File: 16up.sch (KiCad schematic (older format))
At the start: 38 parts, among them CN1 EXPANSION_PORT, CN2 ALMOST_USERPORT, CN3 DB9_MALE, J1 ATTENTION_IN, J2 TAPE_IN, U1 GAL20V8, U102 74LS652, U2 MOS_6529, U3 MOS_6551_ACIA, U4 MAX238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

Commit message: ExtraUserPort -> 16up
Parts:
- CN1: footprint ExtraUserPort:C16_Cart_Conn -> 16up:C16_Cart_Conn
- CN2: footprint ExtraUserPort:24Pin_Edge -> 16up:24Pin_Edge
- CN3: footprint ExtraUserPort:DB_9M -> 16up:DB_9M
- J2: footprint ExtraUserPort:Connector_Mini-DIN_Female_8Pin_2rows -> 16up:Connector_Mini-DIN_Female_8Pin_2rows
- V0: footprint ExtraUserPort:logo -> 16up:logo
- V1: footprint ExtraUserPort:cc_by_nc_sa -> 16up:cc_by_nc_sa
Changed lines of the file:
@@
 encoding utf-8
 Sheet 1 1
-Title "ExtraUserPort"
+Title "16up"
 Date "2022-09-17"
 Rev "1git"
@@
 F 0 "CN2" H 14315 2680 50  0000 C CNN
 F 1 "ALMOST_USERPORT" H 14315 2589 50  0000 C CNN
-F 2 "ExtraUserPort:24Pin_Edge" H 14315 1765 50  0001 C CNN
+F 2 "16up:24Pin_Edge" H 14315 1765 50  0001 C CNN
 F 3 "DOCUMENTATION" H 14315 1765 50  0001 C CNN
 	1    14315 1765
@@
 F 0 "CN3" H 14538 8742 50  0000 C CNN
 F 1 "DB9_MALE" H 14538 8651 50  0000 C CNN
-F 2 "ExtraUserPort:DB_9M" H 14620 8050 50  0001 C CNN
+F 2 "16up:DB_9M" H 14620 8050 50  0001 C CNN
 F 3 " ~" H 14620 8050 50  0001 C CNN
 	1    14620 8050
@@
 F 0 "CN1" H 2435 4370 50  0000 C CNN
 F 1 "EXPANSION_PORT" H 2435 4279 50  0000 C CNN
-F 2 "ExtraUserPort:C16_Cart_Conn" H 2435 1155 50  0001 C CNN
+F 2 "16up:C16_Cart_Conn" H 2435 1155 50  0001 C CNN
 F 3 "DOCUMENTATION" H 2435 1055 50  0001 C CNN
 	1    2435 2805
@@
 F 0 "J2" H 6040 9780 50  0000 C CNN
 F 1 "TAPE_IN" H 6040 9685 50  0000 C CNN
-F 2 "ExtraUserPort:Connector_Mini-DIN_Female_8Pin_2rows" V 5780 10050 50  0001 C CNN
+F 2 "16up:Connector_Mini-DIN_Female_8Pin_2rows" V 5780 10050 50  0001 C CNN
 F 3 "http://service.powerdynamics.com/ec/Catalog17/Section%2011.pdf" V 5780 10050 50  0001 C CNN
 	1    5790 10060
@@
 F 0 "V0" H 11078 11071 50  0000 L CNN
 F 1 "LOGO" H 11078 10980 50  0000 L CNN
-F 2 "ExtraUserPort:logo" H 11000 11025 50  0001 C CNN
+F 2 "16up:logo" H 11000 11025 50  0001 C CNN
 F 3 "" H 11000 11025 50  0001 C CNN
 	1    11000 11025
@@
 F 0 "V1" H 11078 10846 50  0000 L CNN
 F 1 "CC-BY-NC-SA" H 11078 10755 50  0000 L CNN
-F 2 "ExtraUserPort:cc_by_nc_sa" H 11000 10800 50  0001 C CNN
+F 2 "16up:cc_by_nc_sa" H 11000 10800 50  0001 C CNN
 F 3 "" H 11000 10800 50  0001 C CNN
 	1    11000 10800

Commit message: Fix userport connector !!!
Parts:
- CN2: footprint 16up:24Pin_Edge -> 16up:Plus4_UserPort
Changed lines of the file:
@@
 F 0 "CN2" H 14315 2680 50  0000 C CNN
 F 1 "ALMOST_USERPORT" H 14315 2589 50  0000 C CNN
-F 2 "16up:24Pin_Edge" H 14315 1765 50  0001 C CNN
+F 2 "16up:Plus4_UserPort" H 14315 1765 50  0001 C CNN
 F 3 "DOCUMENTATION" H 14315 1765 50  0001 C CNN
 	1    14315 1765

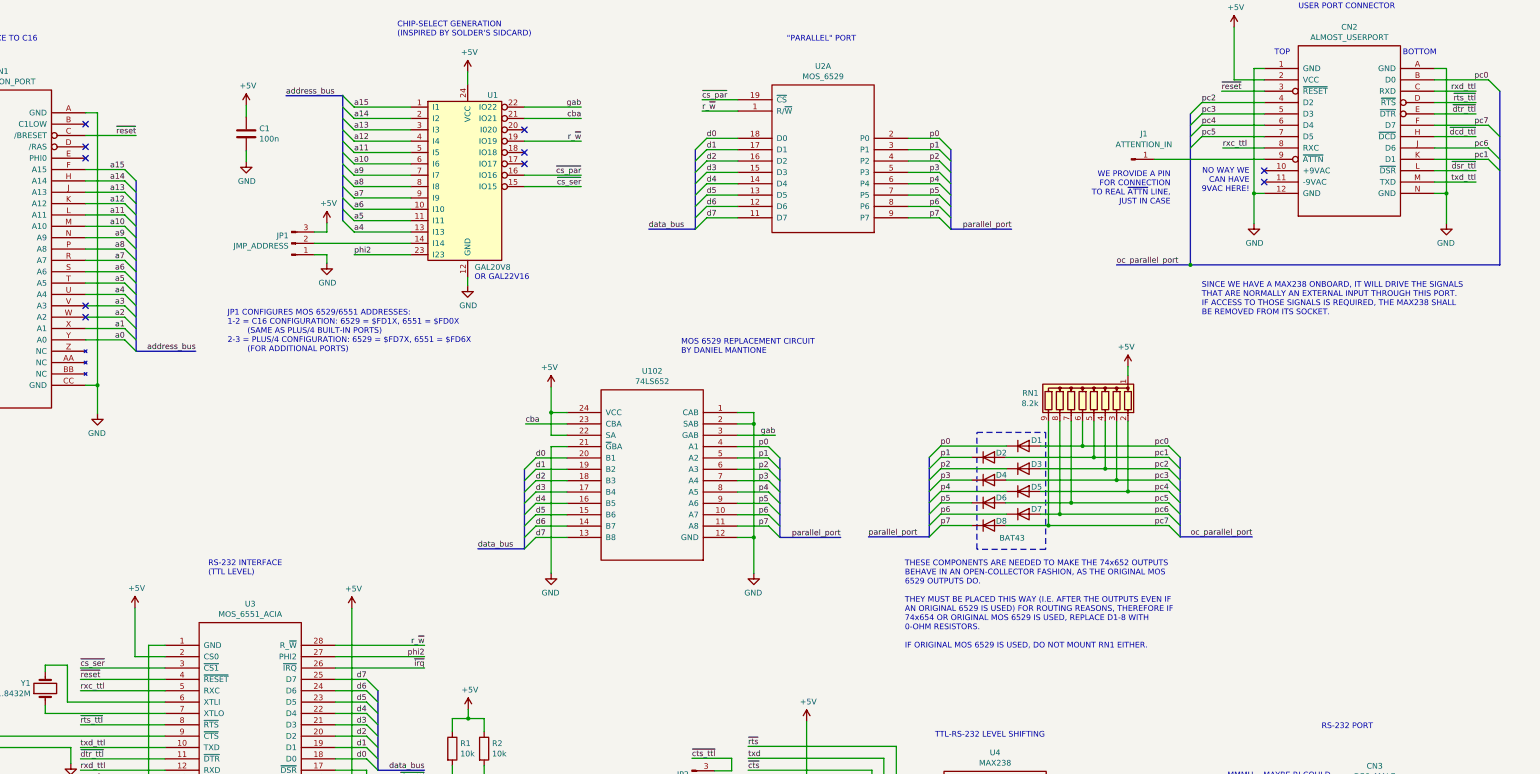
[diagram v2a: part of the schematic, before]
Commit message: Remove serial signals from Userport connector They wouldn't work anyway, as whatever gets connected there expects all control signals to be inverted as per Commodore serial port standards.
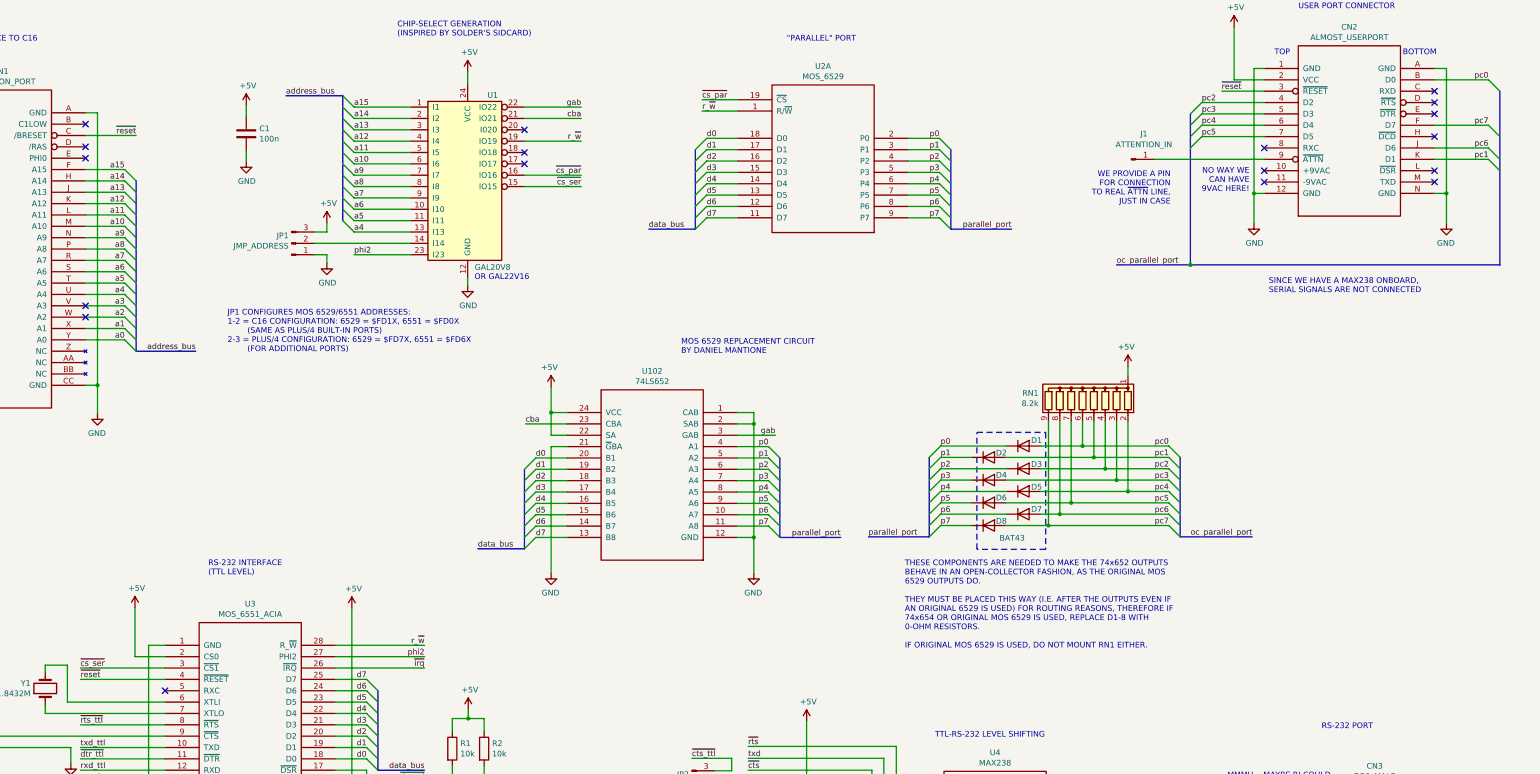
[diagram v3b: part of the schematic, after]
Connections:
- net rxd_ttl: no longer CN2.C (RXD)
- net txd_ttl: no longer CN2.M (TXD)
- net ~dcd_ttl: no longer CN2.H (~DCD)
- net ~dsr_ttl: no longer CN2.L (~DSR)
- net ~dtr_ttl: no longer CN2.E (~DTR)
- net ~rts_ttl: no longer CN2.D (~RTS)
- net rxc_ttl: no longer names the net of CN2.8 (RXC)
- net rxc_ttl: no longer U3.5 (RXC)
- no-connect marks 29 -> 37
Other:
- note added: "SINCE WE HAVE A MAX238 ONBOARD,\nSERIAL SIGNALS ARE NOT CONNECTED"
- note removed: "SINCE WE HAVE A MAX238 ONBOARD, IT WILL DRIVE THE SIGNALS\nTHAT ARE NORMALLY AN EXTERNAL INPUT THROUGH THIS PORT.\nIF ACCESS TO THOSE SIGNALS IS REQUIRED, THE MAX238 SHALL\nBE REMOVED FROM ITS SOCKET."
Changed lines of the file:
@@
 Sheet 1 1
 Title "16up"
-Date "2022-09-17"
+Date "2022-09-21"
 Rev "1git"
 Comp "SukkoPera & The Folks From The Plus/4 World Forum"
@@
 Wire Wire Line
 	14320 8250 13840 8250
-Wire Wire Line
-	15065 1815 15430 1815
-Wire Wire Line
-	15065 2115 15430 2115
-Text Label 15430 1815 2    50   ~ 0
-~dcd_ttl
-Text Label 15430 2115 2    50   ~ 0
-~dsr_ttl
-Wire Wire Line
-	15065 2215 15430 2215
-Text Label 15430 2215 2    50   ~ 0
-txd_ttl
 Wire Wire Line
 	14320 8350 13840 8350
@@
 Text Notes 13865 700  0    50   ~ 0
 USER PORT CONNECTOR
-Wire Wire Line
-	13565 1915 13200 1915
-Text Label 13200 1915 0    50   ~ 0
-rxc_ttl
 Text Notes 10665 7115 0    50   ~ 0
 TTL-RS-232 LEVEL SHIFTING
@@
 Wire Wire Line
 	1240 4005 1580 4005
-Text Label 15430 1615 2    50   ~ 0
-~dtr_ttl
-Text Label 15430 1515 2    50   ~ 0
-~rts_ttl
-Text Label 15430 1415 2    50   ~ 0
-rxd_ttl
-Wire Wire Line
-	15065 1615 15430 1615
-Wire Wire Line
-	15065 1515 15430 1515
-Wire Wire Line
-	15065 1415 15430 1415
-Text Notes 13015 3395 0    50   ~ 0
-SINCE WE HAVE A MAX238 ONBOARD, IT WILL DRIVE THE SIGNALS\nTHAT ARE NORMALLY AN EXTERNAL INPUT THROUGH THIS PORT.\nIF ACCESS TO THOSE SIGNALS IS REQUIRED, THE MAX238 SHALL\nBE REMOVED FROM ITS SOCKET.
+Text Notes 13605 3200 0    50   ~ 0
+SINCE WE HAVE A MAX238 ONBOARD,\nSERIAL SIGNALS ARE NOT CONNECTED
 $Comp
 L Connector:Conn_01x03_Male JP2
@@
 Entry Wire Line
 	3140 7595 3240 7495
-Wire Wire Line
-	3140 6695 3885 6695
-Text Label 3140 6695 0    50   ~ 0
-rxc_ttl
 Wire Wire Line
 	3140 6595 3885 6595
@@
 Text Notes 6350 10750 0    50   ~ 0
 THE IDEA HERE IS TO USE A Y-CABLE AND CONNECT\nTHE DATASSETTE BOTH TO THE ORIGINAL PORT AND TO\nTHIS ONE, SO THAT WE CAN PUT THE SENSE SIGNAL ON\nD2 WHEN REQUIRED.\n\nIDEALLY THE SENSE LINE SHOULD BE BROUGHT HERE\nONLY, BUT PROBABLY IT WON'T HARM ANYWAY.\n\n
+NoConn ~ 13565 1915
+NoConn ~ 15065 1415
+NoConn ~ 15065 1515
+NoConn ~ 15065 1615
+NoConn ~ 15065 1815
+NoConn ~ 15065 2115
+NoConn ~ 15065 2215
+NoConn ~ 3885 6695
 Wire Bus Line
 	15640 1415 15640 2945

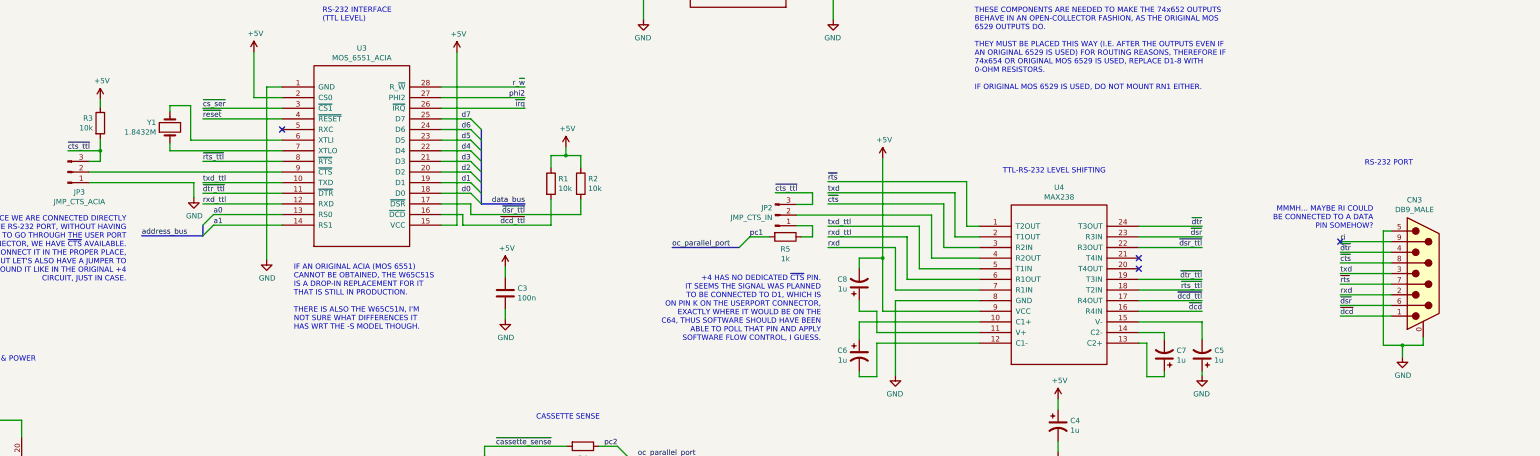
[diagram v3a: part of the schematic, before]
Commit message: Pull-up signals at the RS-232 port
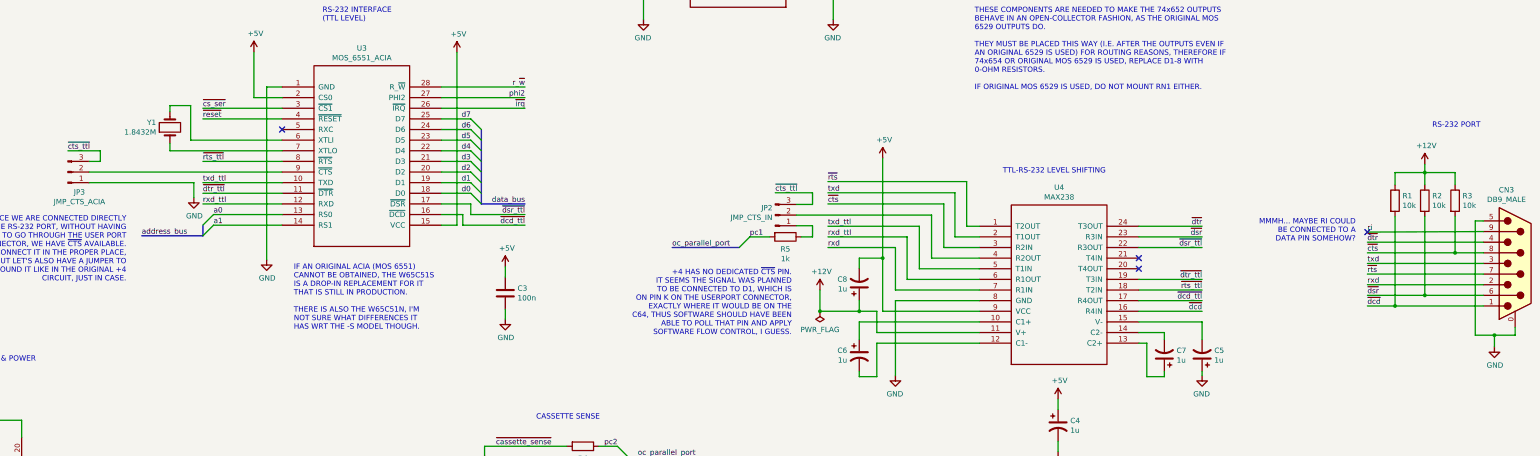
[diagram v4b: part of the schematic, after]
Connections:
- net +5V: no longer R1.1, R2.1, R3.1
- net ~cts: now also R3.2
- net ~cts_ttl: no longer R3.2
- net ~dcd: now also R1.2
- net ~dcd_ttl: no longer R1.2
- net ~dsr: now also R2.2
- net ~dsr_ttl: no longer R2.2
- net +12V: now reaches C8.1, U4.11 (V+)
- net +12V: now also R1.1, R2.1, R3.1
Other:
- note added: "MMMH... MAYBE RI COULD\nBE CONNECTED TO A\nDATA PIN SOMEHOW?"
- note removed: "MMMH... MAYBE RI COULD\nBE CONNECTED TO A DATA\nPIN SOMEHOW?"
- moved on the sheet: CN3, R1, R2, R3
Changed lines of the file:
@@
 Sheet 1 1
 Title "16up"
-Date "2022-09-21"
+Date "2022-09-29"
 Rev "1git"
 Comp "SukkoPera & The Folks From The Plus/4 World Forum"
@@
 L Connector:DB9_Male_MountingHoles CN?
 U 1 1 647E28B3
-P 14620 8050
+P 15485 7955
 AR Path="/647386BE/647E28B3" Ref="CN?"  Part="1"
 AR Path="/647E28B3" Ref="CN3"  Part="1"
-F 0 "CN3" H 14538 8742 50  0000 C CNN
-F 1 "DB9_MALE" H 14538 8651 50  0000 C CNN
-F 2 "16up:DB_9M" H 14620 8050 50  0001 C CNN
-F 3 " ~" H 14620 8050 50  0001 C CNN
-	1    14620 8050
-	1    0    0    -1
-$EndComp
-Wire Wire Line
-	14320 7650 14245 7650
-Wire Wire Line
-	14245 7650 14245 8725
-Wire Wire Line
-	14245 8725 14425 8725
-Wire Wire Line
-	14620 8725 14620 8650
-Wire Wire Line
-	14425 8725 14425 8835
-Connection ~ 14425 8725
-Wire Wire Line
-	14425 8725 14620 8725
+F 0 "CN3" H 15403 8647 50  0000 C CNN
+F 1 "DB9_MALE" H 15403 8556 50  0000 C CNN
+F 2 "16up:DB_9M" H 15485 7955 50  0001 C CNN
+F 3 " ~" H 15485 7955 50  0001 C CNN
+	1    15485 7955
+	1    0    0    -1
+$EndComp
+Wire Wire Line
+	15185 7555 15110 7555
+Wire Wire Line
+	15110 7555 15110 8630
+Wire Wire Line
+	15110 8630 15290 8630
+Wire Wire Line
+	15485 8630 15485 8555
+Wire Wire Line
+	15290 8630 15290 8740
+Connection ~ 15290 8630
+Wire Wire Line
+	15290 8630 15485 8630
 $Comp
 L power:GND #PWR?
 U 1 1 647E28C7
-P 14425 8835
+P 15290 8740
 AR Path="/647386BE/647E28C7" Ref="#PWR?"  Part="1"
 AR Path="/647E28C7" Ref="#PWR0118"  Part="1"
-F 0 "#PWR0118" H 14425 8585 50  0001 C CNN
-F 1 "GND" H 14430 8662 50  0000 C CNN
-F 2 "" H 14425 8835 50  0001 C CNN
-F 3 "" H 14425 8835 50  0001 C CNN
-	1    14425 8835
-	1    0    0    -1
-$EndComp
-Wire Wire Line
-	14320 8050 13840 8050
-Wire Wire Line
-	14320 7950 13840 7950
-Wire Wire Line
-	14320 7750 13840 7750
-Text Label 13840 8450 0    50   ~ 0
+F 0 "#PWR0118" H 15290 8490 50  0001 C CNN
+F 1 "GND" H 15295 8567 50  0000 C CNN
+F 2 "" H 15290 8740 50  0001 C CNN
+F 3 "" H 15290 8740 50  0001 C CNN
+	1    15290 8740
+	1    0    0    -1
+$EndComp
+Wire Wire Line
+	15185 7655 14095 7660
+Text Label 14095 8355 0    50   ~ 0
 ~dcd
-Text Label 13840 8250 0    50   ~ 0
+Text Label 14095 8155 0    50   ~ 0
 rxd
-Text Label 13840 8050 0    50   ~ 0
+Text Label 14095 7955 0    50   ~ 0
 txd
-Text Label 13840 7850 0    50   ~ 0
+Text Label 14095 7755 0    50   ~ 0
 ~dtr
-Text Label 13840 8350 0    50   ~ 0
+Text Label 14095 8255 0    50   ~ 0
 ~dsr
-Text Label 13840 8150 0    50   ~ 0
+Text Label 14095 8055 0    50   ~ 0
 ~rts
-Text Label 13840 7950 0    50   ~ 0
+Text Label 14095 7855 0    50   ~ 0
 ~cts
-Text Label 13840 7750 0    50   ~ 0
+Text Label 14095 7660 0    50   ~ 0
 ri
-NoConn ~ 13840 7750
-Wire Wire Line
-	14320 7850 13840 7850
-Wire Wire Line
-	14320 8150 13840 8150
-Wire Wire Line
-	14320 8250 13840 8250
-Wire Wire Line
-	14320 8350 13840 8350
-Wire Wire Line
-	14320 8450 13840 8450
+NoConn ~ 14095 7660
 Connection ~ 12915 2945
 Wire Wire Line
@@
 Text Notes 10665 7115 0    50   ~ 0
 TTL-RS-232 LEVEL SHIFTING
-Text Notes 14070 7040 0    50   ~ 0
+Text Notes 14705 6685 0    50   ~ 0
 RS-232 PORT
 Text Notes 13435 2310 2    50   ~ 0
@@
 	1    0    0    1
 $EndComp
-Text Notes 14150 7635 2    50   ~ 0
-MMMH... MAYBE RI COULD\nBE CONNECTED TO A DATA\nPIN SOMEHOW?
+Text Notes 13985 7755 2    50   ~ 0
+MMMH... MAYBE RI COULD\nBE CONNECTED TO A\nDATA PIN SOMEHOW?
 Wire Wire Line
 	8725 7400 8875 7400
@@
 Text Label 7555 7805 0    50   ~ 0
 oc_parallel_port
-Text Notes 8955 8690 2    50   ~ 0
+Text Notes 8680 8635 2    50   ~ 0
 +4 HAS NO DEDICATED ~CTS~ PIN.\nIT SEEMS THE SIGNAL WAS PLANNED\nTO BE CONNECTED TO D1, WHICH IS\nON PIN K ON THE USERPORT CONNECTOR,\nEXACTLY WHERE IT WOULD BE ON THE\nC64, THUS SOFTWARE SHOULD HAVE BEEN\nABLE TO POLL THAT PIN AND APPLY\nSOFTWARE FLOW CONTROL, I GUESS.
 Wire Wire Line
@@
 Wire Wire Line
 	5660 7395 5660 7495
-$Comp
-L power:+5V #PWR0126
-U 1 1 6524739E
-P 6555 6860
-F 0 "#PWR0126" H 6555 6710 50  0001 C CNN
-F 1 "+5V" H 6570 7033 50  0000 C CNN
-F 2 "" H 6555 6860 50  0001 C CNN
-F 3 "" H 6555 6860 50  0001 C CNN
-	1    6555 6860
-	1    0    0    -1
-$EndComp
-Wire Wire Line
-	6555 6940 6695 6940
-Connection ~ 6555 6940
-Wire Wire Line
-	6555 6940 6555 6860
-Wire Wire Line
-	6695 6940 6695 7055
-Wire Wire Line
-	6415 6940 6555 6940
-Wire Wire Line
-	6415 7055 6415 6940
-Wire Wire Line
-	6415 7355 6415 7595
+Wire Wire Line
+	14355 7215 14355 7100
 Wire Wire Line
 	5530 5970 5530 7595
-Wire Wire Line
-	6695 7355 6695 7495
 $Comp
 L Device:R R2
 U 1 1 64D53226
-P 6695 7205
-F 0 "R2" H 6765 7251 50  0000 L CNN
-F 1 "10k" H 6765 7160 50  0000 L CNN
-F 2 "Resistor_THT:R_Axial_DIN0207_L6.3mm_D2.5mm_P2.54mm_Vertical" V 6625 7205 50  0001 C CNN
-F 3 "~" H 6695 7205 50  0001 C CNN
-	1    6695 7205
+P 14635 7365
+F 0 "R2" H 14705 7411 50  0000 L CNN
+F 1 "10k" H 14705 7320 50  0000 L CNN
+F 2 "Resistor_THT:R_Axial_DIN0207_L6.3mm_D2.5mm_P2.54mm_Vertical" V 14565 7365 50  0001 C CNN
+F 3 "~" H 14635 7365 50  0001 C CNN
+	1    14635 7365
 	1    0    0    -1
 $EndComp
@@
 L Device:R R1
 U 1 1 64D5229C
-P 6415 7205
-F 0 "R1" H 6485 7251 50  0000 L CNN
-F 1 "10k" H 6485 7160 50  0000 L CNN
-F 2 "Resistor_THT:R_Axial_DIN0207_L6.3mm_D2.5mm_P2.54mm_Vertical" V 6345 7205 50  0001 C CNN
-F 3 "~" H 6415 7205 50  0001 C CNN
-	1    6415 7205
+P 14355 7365
+F 0 "R1" H 14425 7411 50  0000 L CNN
+F 1 "10k" H 14425 7320 50  0000 L CNN
+F 2 "Resistor_THT:R_Axial_DIN0207_L6.3mm_D2.5mm_P2.54mm_Vertical" V 14285 7365 50  0001 C CNN
+F 3 "~" H 14355 7365 50  0001 C CNN
+	1    14355 7365
 	1    0    0    -1
 $EndComp
@@
 	3140 7295 3885 7295
 Wire Wire Line
-	5660 7495 6695 7495
-Wire Wire Line
 	5385 7495 5585 7495
 Wire Wire Line
 	5585 7495 5585 7595
-Wire Wire Line
-	5585 7595 6415 7595
 Text Notes 765  8885 0    50   ~ 0
 DECOUPLING & POWER
@@
 $EndComp
 $Comp
-L power:+5V #PWR03
-U 1 1 634892F5
-P 2175 6410
-F 0 "#PWR03" H 2175 6260 50  0001 C CNN
-F 1 "+5V" H 2190 6583 50  0000 C CNN
-F 2 "" H 2175 6410 50  0001 C CNN
-F 3 "" H 2175 6410 50  0001 C CNN
-	1    2175 6410
-	1    0    0    -1
-$EndComp
-Wire Wire Line
-	2175 6410 2175 6485
-Wire Wire Line
-	2175 6785 2175 6895
-$Comp
 L Device:R R3
 U 1 1 63489861
-P 2175 6635
-F 0 "R3" H 2105 6681 50  0000 R CNN
-F 1 "10k" H 2105 6590 50  0000 R CNN
-F 2 "Resistor_THT:R_Axial_DIN0207_L6.3mm_D2.5mm_P2.54mm_Vertical" V 2105 6635 50  0001 C CNN
-F 3 "~" H 2175 6635 50  0001 C CNN
-	1    2175 6635
+P 14920 7365
+F 0 "R3" H 14990 7411 50  0000 L CNN
+F 1 "10k" H 14990 7320 50  0000 L CNN
+F 2 "Resistor_THT:R_Axial_DIN0207_L6.3mm_D2.5mm_P2.54mm_Vertical" V 14850 7365 50  0001 C CNN
+F 3 "~" H 14920 7365 50  0001 C CNN
+	1    14920 7365
 	1    0    0    -1
 $EndComp
@@
 Wire Wire Line
 	2175 6895 1870 6895
-Connection ~ 2175 6895
 Text Notes 13655 1105 0    50   ~ 0
 TOP
@@
 NoConn ~ 15065 2215
 NoConn ~ 3885 6695
+Wire Wire Line
+	14095 7855 14920 7855
+Wire Wire Line
+	14095 7955 15185 7955
+Wire Wire Line
+	14095 8055 15185 8055
+Wire Wire Line
+	14095 8155 15185 8155
+Wire Wire Line
+	14095 8255 14635 8255
+Wire Wire Line
+	14095 8355 14355 8355
+Wire Wire Line
+	14635 7515 14635 8255
+Connection ~ 14635 8255
+Wire Wire Line
+	14635 8255 15185 8255
+Connection ~ 14355 8355
+Wire Wire Line
+	14355 8355 15185 8355
+Wire Wire Line
+	14355 7515 14355 8355
+Wire Wire Line
+	14095 7755 15185 7755
+Wire Wire Line
+	14920 7515 14920 7855
+Connection ~ 14920 7855
+Wire Wire Line
+	14920 7855 15185 7855
+Wire Wire Line
+	14355 7100 14635 7100
+Wire Wire Line
+	14920 7100 14920 7215
+Wire Wire Line
+	14635 7215 14635 7100
+Connection ~ 14635 7100
+Wire Wire Line
+	14635 7100 14920 7100
+Wire Wire Line
+	14635 7100 14635 7020
+$Comp
+L power:+12V #PWR0130
+U 1 1 63AE2B0B
+P 14635 7020
+F 0 "#PWR0130" H 14635 6870 50  0001 C CNN
+F 1 "+12V" H 14650 7193 50  0000 C CNN
+F 2 "" H 14635 7020 50  0001 C CNN
+F 3 "" H 14635 7020 50  0001 C CNN
+	1    14635 7020
+	1    0    0    -1
+$EndComp
+Wire Wire Line
+	5660 7495 6170 7495
+Wire Wire Line
+	5585 7595 6170 7595
+Wire Wire Line
+	9315 8405 8945 8405
+Wire Wire Line
+	8945 8405 8945 8205
+$Comp
+L power:+12V #PWR0126
+U 1 1 637F1E1A
+P 8945 8205
+F 0 "#PWR0126" H 8945 8055 50  0001 C CNN
+F 1 "+12V" H 8960 8378 50  0000 C CNN
+F 2 "" H 8945 8205 50  0001 C CNN
+F 3 "" H 8945 8205 50  0001 C CNN
+	1    8945 8205
+	1    0    0    -1
+$EndComp
+$Comp
+L power:PWR_FLAG #FLG0103
+U 1 1 637F2C47
+P 8945 8405
+F 0 "#FLG0103" H 8945 8480 50  0001 C CNN
+F 1 "PWR_FLAG" H 8945 8578 50  0000 C CNN
+F 2 "" H 8945 8405 50  0001 C CNN
+F 3 "~" H 8945 8405 50  0001 C CNN
+	1    8945 8405
+	-1   0    0    1
+$EndComp
+Connection ~ 8945 8405
+Connection ~ 9315 8405
 Wire Bus Line
 	15640 1415 15640 2945
